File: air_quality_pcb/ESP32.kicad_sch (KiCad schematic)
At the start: 1 part, among them U1 XIAO-ESP32-C6

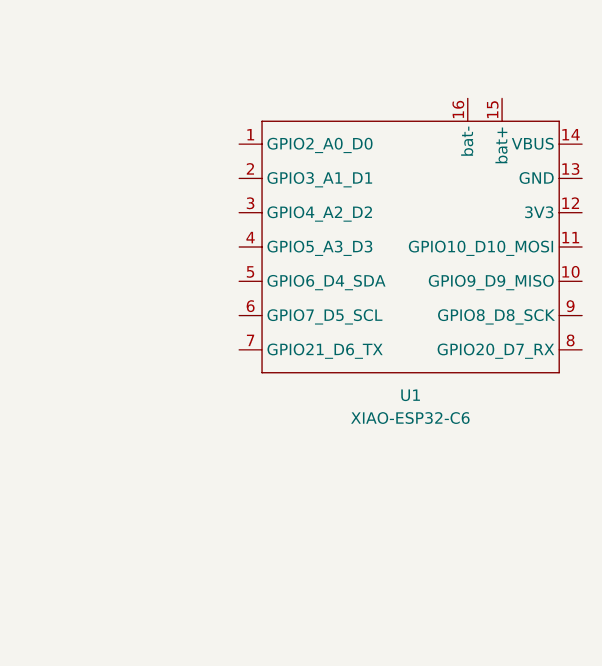
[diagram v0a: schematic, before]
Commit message: added sensors and display example
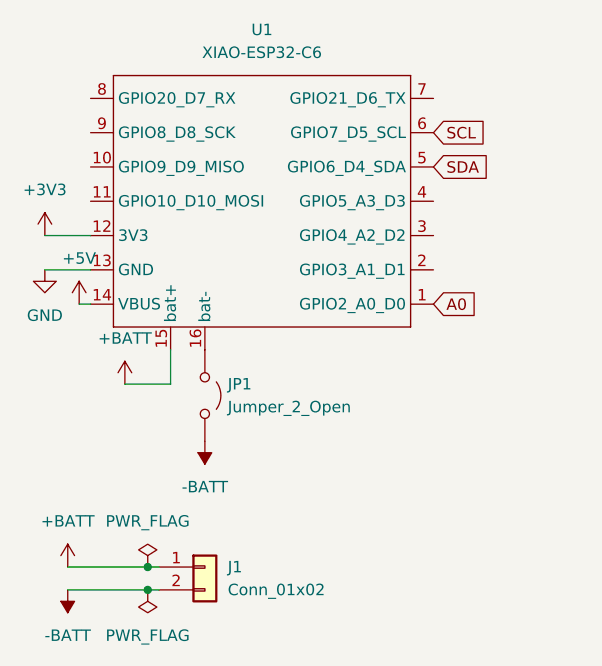
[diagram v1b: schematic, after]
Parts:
- added J1: Conn_01x02, project_extras:BATT_connector, symbol Connector_Generic:Conn_01x02
- added JP1: Jumper_2_Open, Jumper:SolderJumper-2_P1.3mm_Open_RoundedPad1.0x1.5mm, symbol Jumper:Jumper_2_Open
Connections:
- net A0: now reaches U1.1 (GPIO2_A0_D0)
- net +3V3: now reaches U1.12 (3V3)
- net GND: now reaches U1.13 (GND)
- net +5V: now reaches U1.14 (VBUS)
- net +BATT: now reaches U1.15 (bat+)
- net +BATT: now also J1.1 (Pin_1)
- net at U1.16 (bat-): now also JP1.1 (A)
- net SDA: now reaches U1.5 (GPIO6_D4_SDA)
- net SCL: now reaches U1.6 (GPIO7_D5_SCL)
- new net -BATT: J1.2 (Pin_2), JP1.2 (B)
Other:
- moved on the sheet: U1

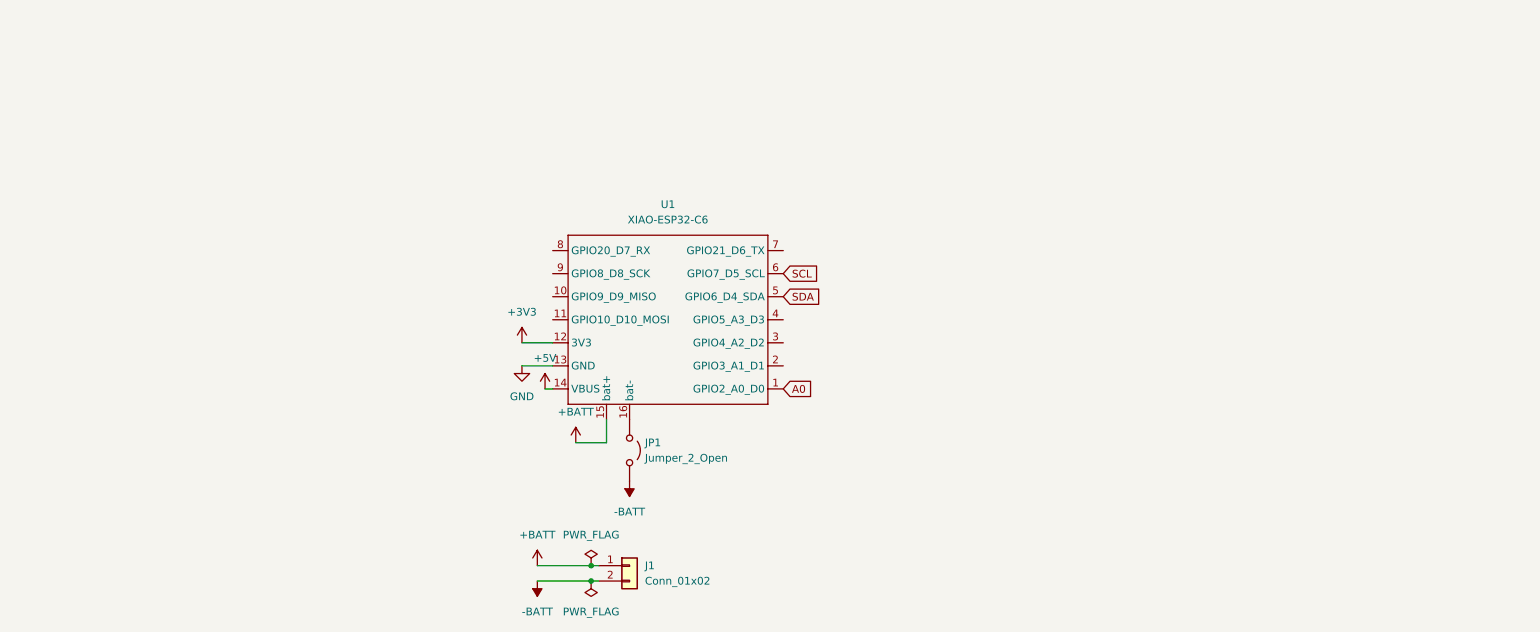
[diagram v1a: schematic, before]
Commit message: added mq7 sensor and display connector
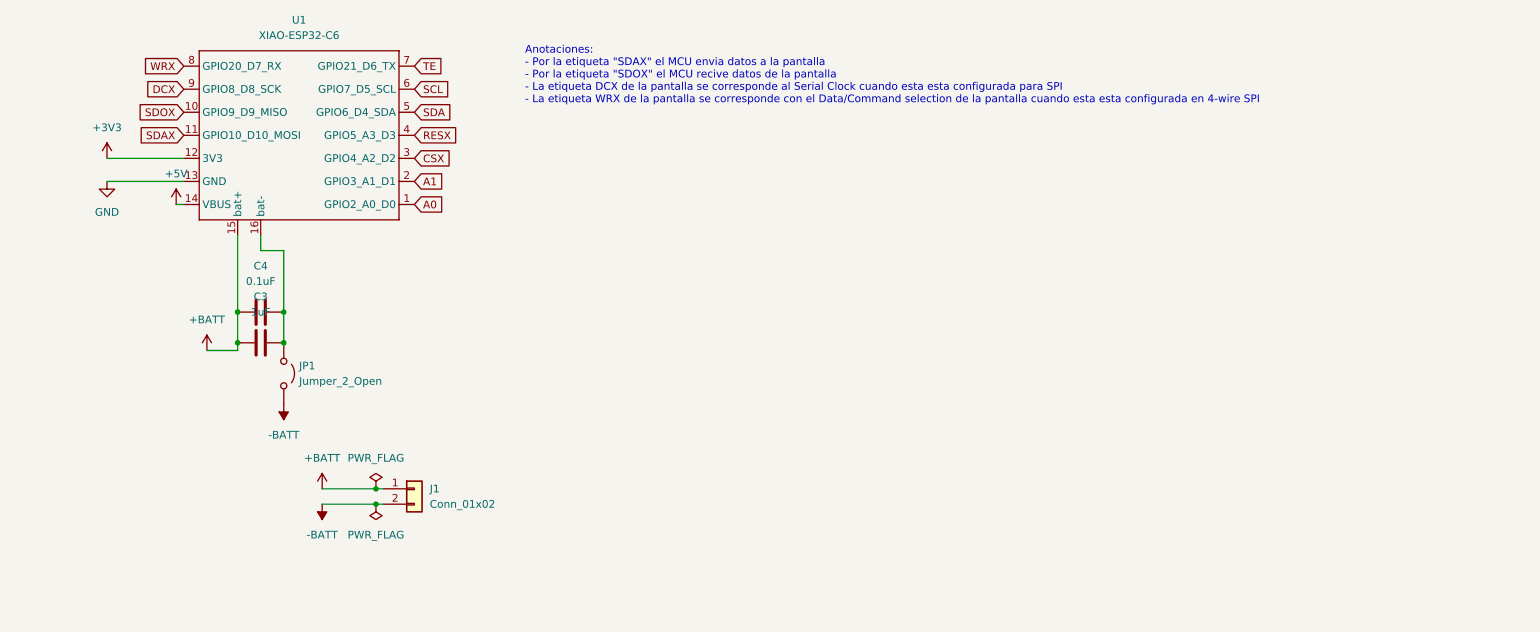
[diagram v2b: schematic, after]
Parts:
- added C3: 1uF, Capacitor_SMD:C_1206_3216Metric, symbol Device:C
- added C4: 0.1uF, Capacitor_SMD:C_1206_3216Metric, symbol Device:C
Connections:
- net +BATT: now also C3.1, C4.1
- net at JP1.1 (A), U1.16 (bat-): now also C3.2, C4.2
- net SDOX: now reaches U1.10 (GPIO9_D9_MISO)
- net SDAX: now reaches U1.11 (GPIO10_D10_MOSI)
- net A1: now reaches U1.2 (GPIO3_A1_D1)
- net CSX: now reaches U1.3 (GPIO4_A2_D2)
- net RESX: now reaches U1.4 (GPIO5_A3_D3)
- net TE: now reaches U1.7 (GPIO21_D6_TX)
- net WRX: now reaches U1.8 (GPIO20_D7_RX)
- net DCX: now reaches U1.9 (GPIO8_D8_SCK)
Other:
- note added: "Anotaciones: - Por la etiqueta "SDAX" el MCU envia datos a la pantalla - Por la etiqueta "SDOX" el MCU recive datos de la pantalla - La etiqueta DCX de la pantalla se corresponde al Serial Clock cuando esta esta configurada para SPI - La etiqueta WRX de la pantalla se corresponde con el Data/Command selection de la pantalla cuando esta esta configurada en 4-wire SPI"
- moved on the sheet: J1, JP1, U1

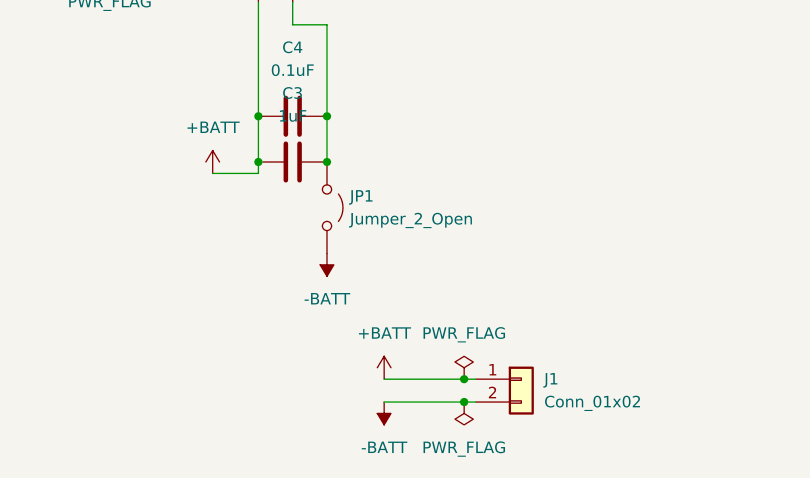
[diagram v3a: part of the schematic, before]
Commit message: added buck boost for 5v battery powered
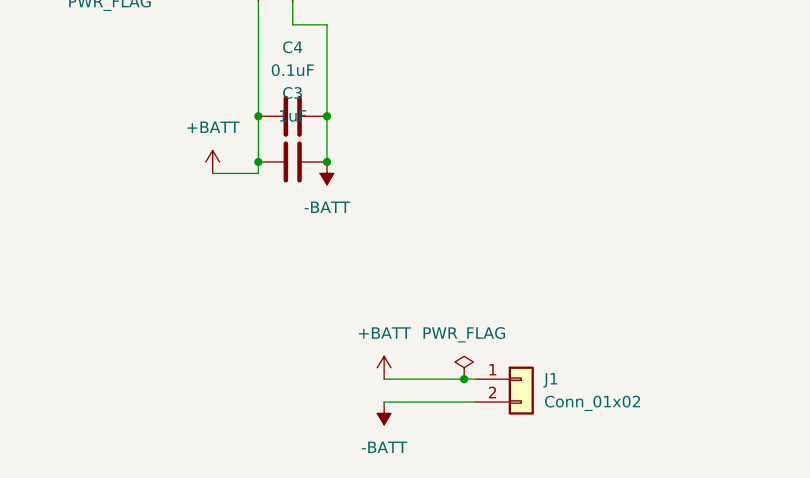
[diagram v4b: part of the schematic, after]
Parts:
- removed JP1: Jumper_2_Open, Jumper:SolderJumper-2_P1.3mm_Open_RoundedPad1.0x1.5mm, symbol Jumper:Jumper_2_Open
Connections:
- net -BATT: now also C3.2, C4.2, U1.16 (bat-)
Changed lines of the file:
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@@
+	)
+	(junction
+		(at 69.85 86.36)
+		(diameter 0)
+		(color 0 0 0 0)
+	)
+	(junction
+		(at 35.56 60.96)
+		(diameter 0)
+		(color 0 0 0 0)
+	)
+	(junction
+		(at 85.09 115.57)
+		(diameter 0)
+		(color 0 0 0 0)
 	)
 	(junction
@@
 	)
 	(junction
-		(at 69.85 86.36)
-		(diameter 0)
-		(color 0 0 0 0)
-	)
-	(junction
-		(at 35.56 60.96)
-		(diameter 0)
-		(color 0 0 0 0)
-	)
-	(junction
-		(at 85.09 115.57)
-		(diameter 0)
-		(color 0 0 0 0)
-	)
-	(junction
 		(at 62.23 91.44)
 		(diameter 0)
@@
 		(color 0 0 0 0)
 	)
-	(junction
-		(at 85.09 118.11)
-		(diameter 0)
-		(color 0 0 0 0)
-	)
 	(wire
 		(pts
@@
 	(wire
 		(pts
-			(xy 85.09 118.11) (xy 86.36 118.11)
-		)
-		(stroke
-			(width 0)
-			(type default)
-		)
-	)
-	(wire
-		(pts
 			(xy 27.94 60.96) (xy 35.56 60.96)
 		)
@@
 	(wire
 		(pts
-			(xy 76.2 118.11) (xy 85.09 118.11)
+			(xy 76.2 118.11) (xy 86.36 118.11)
 		)
 		(stroke
@@
 	(symbol
 		(lib_id "power:-BATT")
-		(at 69.85 101.6 180)
+		(at 69.85 91.44 180)
 		(unit 1)
 		(exclude_from_sim no)
@@
 		(fields_autoplaced yes)
 		(property "Reference" "#PWR07"
-			(at 69.85 97.79 0)
+			(at 69.85 87.63 0)
 			(effects
 				(font
@@
 		)
 		(property "Value" "-BATT"
-			(at 69.85 106.68 0)
+			(at 69.85 96.52 0)
 			(effects
 				(font
@@
 		)
 		(property "Footprint" ""
-			(at 69.85 101.6 0)
+			(at 69.85 91.44 0)
 			(effects
 				(font
@@
 		)
 		(property "Datasheet" ""
-			(at 69.85 101.6 0)
+			(at 69.85 91.44 0)
 			(effects
 				(font
@@
 		)
 		(property "Description" "Power symbol creates a global label with name \"-BATT\""
-			(at 69.85 101.6 0)
+			(at 69.85 91.44 0)
 			(effects
 				(font
@@
 					(unit 1)
 				)
-			)
-		)
-	)
-	(symbol
-		(lib_id "Jumper:Jumper_2_Open")
-		(at 69.85 96.52 270)
-		(unit 1)
-		(exclude_from_sim no)
-		(in_bom yes)
-		(on_board yes)
-		(dnp no)
-		(fields_autoplaced yes)
-		(property "Reference" "JP1"
-			(at 72.39 95.2499 90)
-			(effects
-				(font
-					(size 1.27 1.27)
-				)
-				(justify left)
-			)
-		)
-		(property "Value" "Jumper_2_Open"
-			(at 72.39 97.7899 90)
-			(effects
-				(font
-					(size 1.27 1.27)
-				)
-				(justify left)
-			)
-		)
-		(property "Footprint" "Jumper:SolderJumper-2_P1.3mm_Open_RoundedPad1.0x1.5mm"
-			(at 69.85 96.52 0)
-			(effects
-				(font
-					(size 1.27 1.27)
-				)
-				(hide yes)
-			)
-		)
-		(property "Datasheet" "~"
-			(at 69.85 96.52 0)
-			(effects
-				(font
-					(size 1.27 1.27)
-				)
-				(hide yes)
-			)
-		)
-		(property "Description" "Jumper, 2-pole, open"
-			(at 69.85 96.52 0)
-			(effects
-				(font
-					(size 1.27 1.27)
-				)
-				(hide yes)
-			)
-		)
-		(pin "1"
-		)
-		(pin "2"
-		)
-		(instances
-			(project "air_quality_pcb"
-				(path "/be1998fb-5191-483f-bd03-46c23a7136b7/d57d56af-76e6-4004-8c91-b6d59a7a3d21"
-					(reference "JP1")
-					(unit 1)
-				)
-			)
-		)
-	)
-	(symbol
-		(lib_id "power:PWR_FLAG")
-		(at 85.09 118.11 180)
-		(unit 1)
-		(exclude_from_sim no)
-		(in_bom yes)
-		(on_board yes)
-		(dnp no)
-		(fields_autoplaced yes)
-		(property "Reference" "#FLG02"
-			(at 85.09 120.015 0)
-			(effects
-				(font
-					(size 1.27 1.27)
-				)
-				(hide yes)
-			)
-		)
-		(property "Value" "PWR_FLAG"
-			(at 85.09 123.19 0)
-			(effects
-				(font
-					(size 1.27 1.27)
-				)
-			)
-		)
-		(property "Footprint" ""
-			(at 85.09 118.11 0)
-			(effects
-				(font
-					(size 1.27 1.27)
-				)
-				(hide yes)
-			)
-		)
-		(property "Datasheet" "~"
-			(at 85.09 118.11 0)
-			(effects
-				(font
-					(size 1.27 1.27)
-				)
-				(hide yes)
-			)
-		)
-		(property "Description" "Special symbol for telling ERC where power comes from"
-			(at 85.09 118.11 0)
-			(effects
-				(font
-					(size 1.27 1.27)
-				)
-				(hide yes)
-			)
-		)
-		(pin "1"
-		)
-		(instances
-			(project "air_quality_pcb"
-				(path "/be1998fb-5191-483f-bd03-46c23a7136b7/d57d56af-76e6-4004-8c91-b6d59a7a3d21"
-					(reference "#FLG02")
-					(unit 1)
-				)

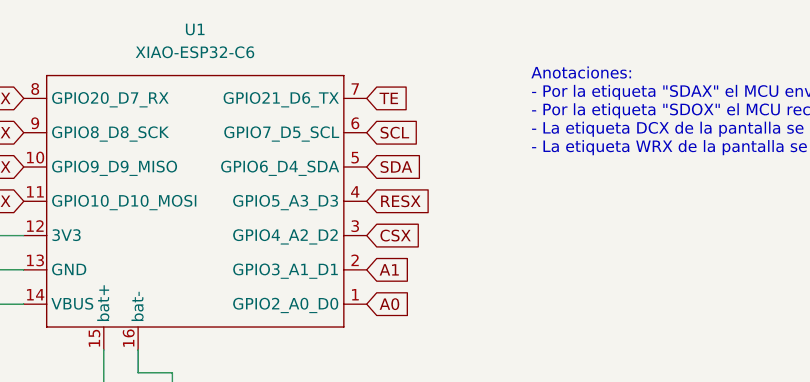
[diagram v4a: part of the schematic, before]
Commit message: added buzzer
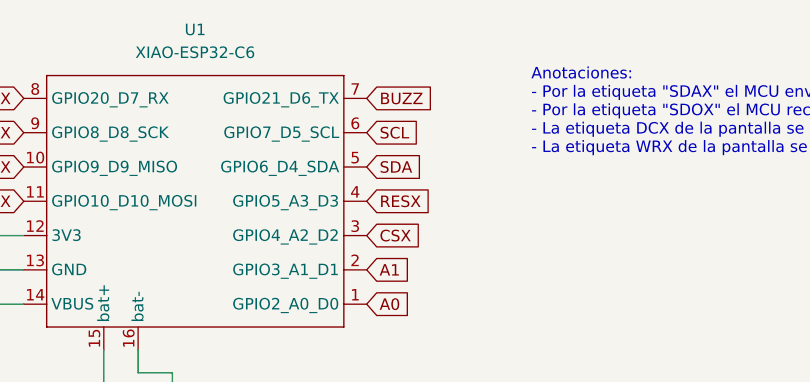
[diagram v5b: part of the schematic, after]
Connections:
- net TE renamed BUZZ
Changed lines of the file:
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@@
+		)
+	)
+	(global_label "BUZZ"
+		(shape input)
+		(at 91.44 45.72 0)
+		(fields_autoplaced yes)
+		(effects
+			(font
+				(size 1.27 1.27)
+			)
+			(justify left)
+		)
+		(property "Intersheetrefs" "${INTERSHEET_REFS}"
+			(at 99.4447 45.72 0)
+			(effects
+				(font
+					(size 1.27 1.27)
+				)
+				(justify left)
+				(hide yes)
+			)
 		)
 	)
@@
 				(hide yes)
 			)
-		)
-	)
-	(global_label "TE"
-		(shape input)
-		(at 91.44 45.72 0)
-		(fields_autoplaced yes)
-		(effects
-			(font
-				(size 1.27 1.27)
-			)
-			(justify left)
-		)
-		(property "Intersheetrefs" "${INTERSHEET_REFS}"
-			(at 96.5418 45.72 0)
-			(effects
-				(font
-					(size 1.27 1.27)
-				)
-				(justify left)
-				(hide yes)
-			)
